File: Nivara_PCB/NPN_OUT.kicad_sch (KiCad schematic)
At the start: 9 parts, among them Q1 IRLML0040, U8 LTV-357T

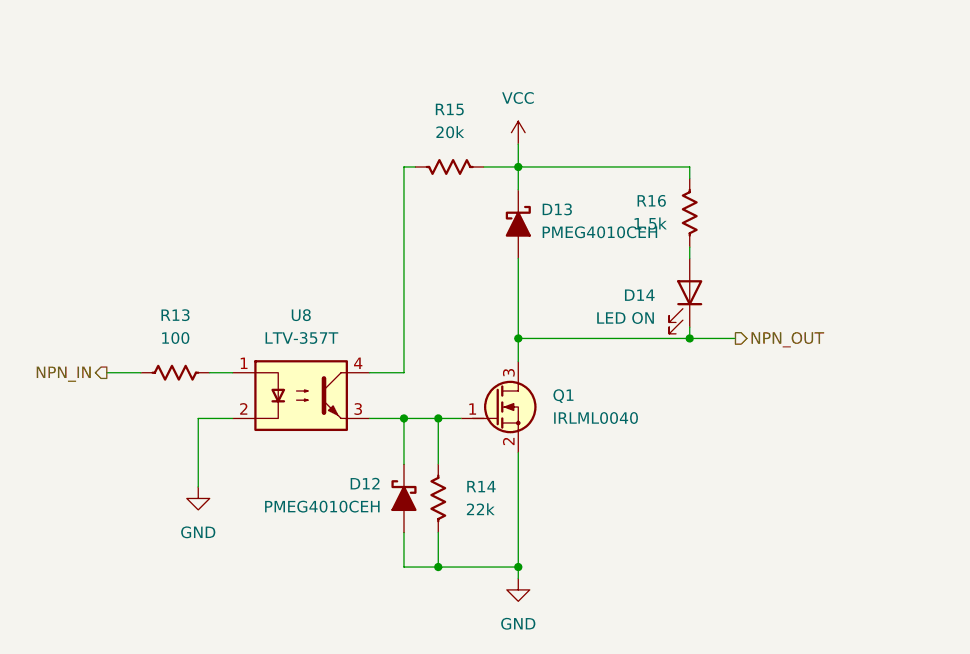
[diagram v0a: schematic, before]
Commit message: Cambios realizados en los archivos de Nivara_PCB.
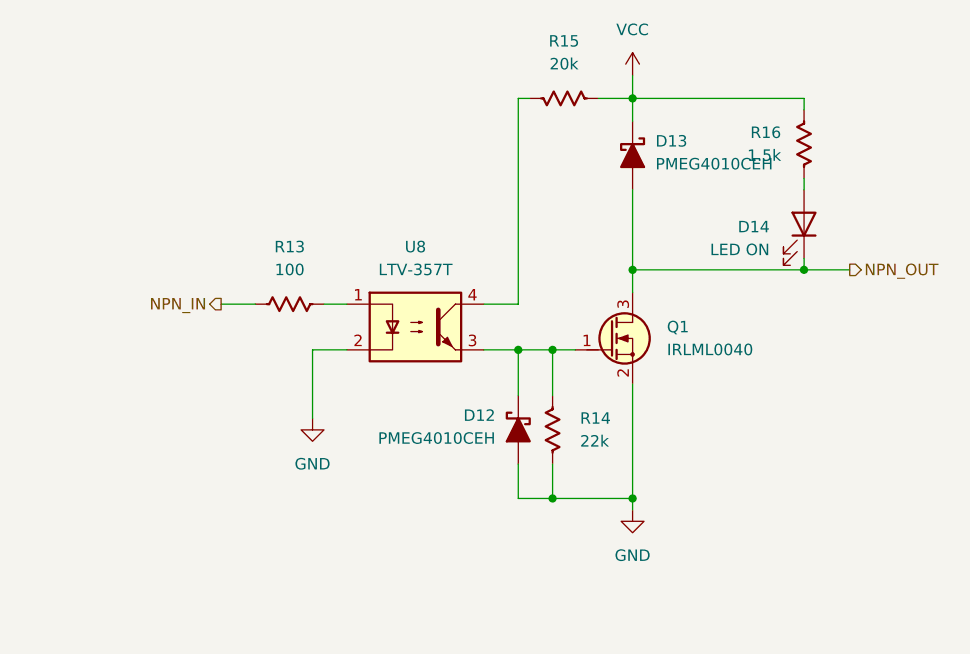
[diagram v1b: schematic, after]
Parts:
- D12, D13: symbol PCM_Diode_Schottky_AKL:PMEG4010CEH -> EasyEDA:PMEG4010CEH
- D14: symbol Device:LED -> EasyEDA:LED
- Q1: symbol PCM_Transistor_MOSFET_AKL:IRLML0040 -> EasyEDA:IRLML0040
- R13, R14, R15, R16: symbol PCM_Resistor_US_AKL:R_0603 -> EasyEDA:R_0603
- U8: symbol Isolator:LTV-357T -> EasyEDA:LTV-357T
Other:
- moved on the sheet: D12, D13, D14, Q1, R13, R14, R15, R16, U8
